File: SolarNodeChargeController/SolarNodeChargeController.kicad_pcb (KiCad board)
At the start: 2 copper layers, 60 x 29 mm, 36 parts, among them J1 Solar_5V, J2 Solar_5V, J3 Solar_5V, J4 Solar_5V, J5 LiPo_1S_4.2V, J6 VOUT, J7 SW_BATT, J8 SW_LOAD, J9 I2C_MCU, Q1 AO3401A, SW3 SOLAR / BATT, U1 CN3791, U2 INA219AID

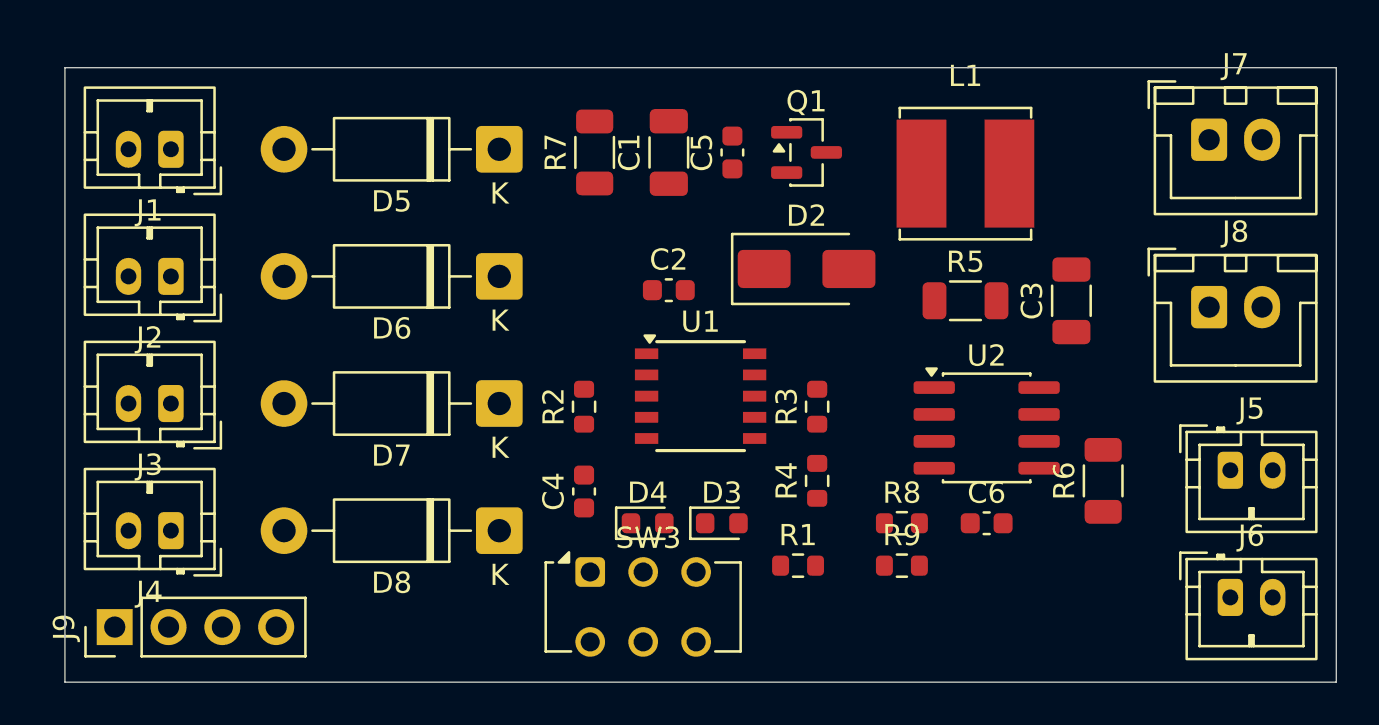
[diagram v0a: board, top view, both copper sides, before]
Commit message: feat: shrink board to 42x26 mm with SMD diodes and 1.25 mm connectors
Input diodes: D5-D8 move from DO-41 1N5819 to SOD-323 1N5819WS (same
40V/1A rating and pinout). The panels peak at ~200-300 mA each, so the
large through-hole part bought nothing and cost ~12 mm of board width.

Connectors: every power connector (solar J1-J4, battery J5, VOUT J6,
switch leads J7/J8) becomes a 2-pin Micro JST 1.25 / Molex PicoBlade
vertical header (53047-0210), and the I2C header J9 a 4-pin one
(53047-0410). The trade-off is that power connectors are no longer
keyed against each other, so the docs call for clear silkscreen labels.

Charge current: R5 0.12R -> 0.15R lowers it from 1.0 A to 0.8 A, leaving
margin on the 1.0 A-rated PicoBlade contacts on the battery path.

The placement draft is rebuilt around the smaller parts: 60x29 -> 42x26
mm, 0 courtyard overlaps, 0 schematic-parity issues, ERC clean.

gen-schematic.js now derives UUIDs from each item's identity (symbol
ref, wire endpoints, label name and position) instead of random ones.
Regenerating an unchanged design is byte-identical, and symbol UUIDs,
which the PCB footprints link to, no longer churn on every run.

README, CLAUDE.md and the README images are updated to match. The
.kicad_pro change is KiCad writing its default settings when the
project was opened.

Co-Authored-By: Claude Opus 5.5 <noreply@anthropic.com>
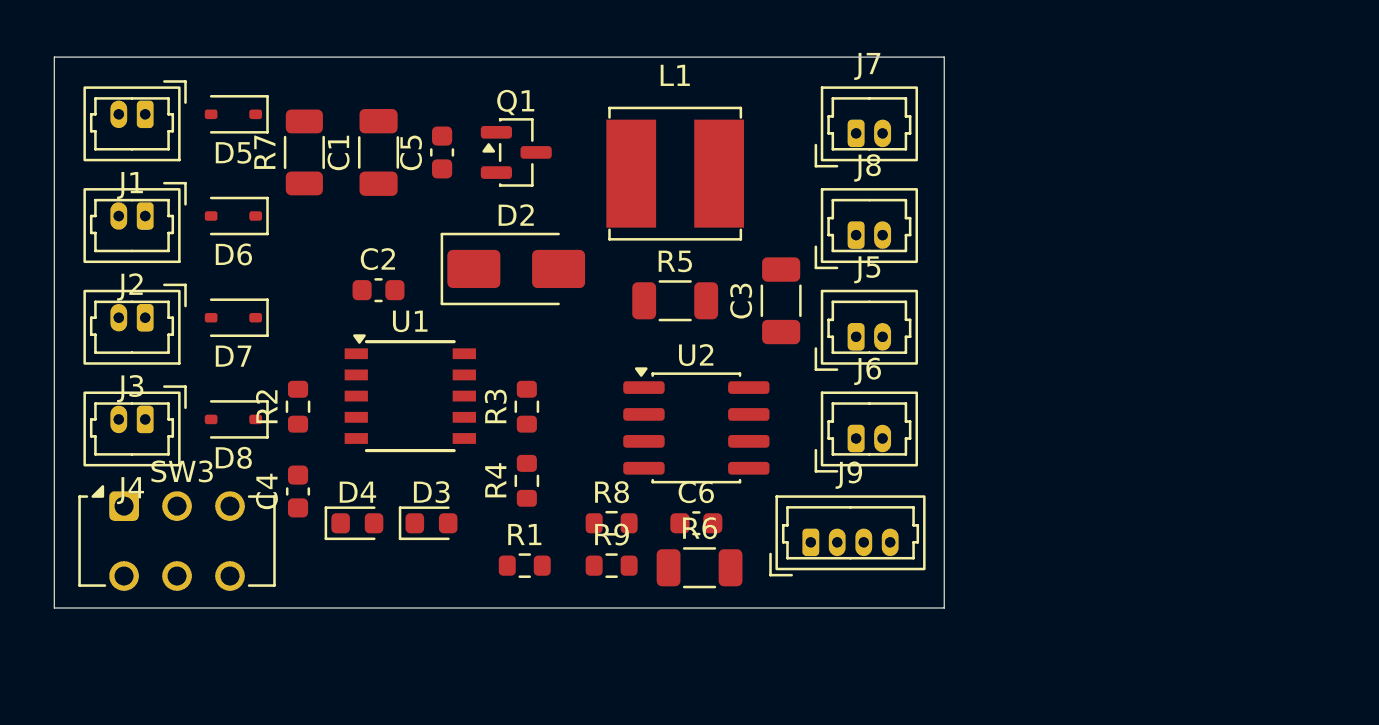
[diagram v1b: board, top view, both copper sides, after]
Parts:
- D5, D6, D7, D8: value 1N5819 -> 1N5819WS; footprint Diode_THT:D_DO-41_SOD81_P10.16mm_Horizontal -> Diode_SMD:D_SOD-323
- J1, J2, J3, J4, J5, J6: footprint Connector_JST:JST_PH_B2B-PH-K_1x02_P2.00mm_Vertical -> Connector_Molex:Molex_PicoBlade_53047-0210_1x02_P1.25mm_Vertical
- J7, J8: footprint Connector_JST:JST_XH_B2B-XH-A_1x02_P2.50mm_Vertical -> Connector_Molex:Molex_PicoBlade_53047-0210_1x02_P1.25mm_Vertical
- J9: footprint Connector_PinHeader_2.54mm:PinHeader_1x04_P2.54mm_Vertical -> Connector_Molex:Molex_PicoBlade_53047-0410_1x04_P1.25mm_Vertical
- R5: value 0.12R 1% -> 0.15R 1%
- moved J9 33.1 mm to (135.2, 122.4), turned to 0 degrees
- moved SW3 22.2 mm to (102.8, 120.7)
- moved R6 19.5 mm to (129.9, 123.6), turned to 0 degrees
- moved J6 19.2 mm to (137.3, 117.5)
- moved J5 18.8 mm to (137.3, 112.7)
- moved J8 17.0 mm to (137.3, 107.9)
- moved J7 16.7 mm to (137.3, 103.1)
- moved C1 13.7 mm to (114.8, 104.0)
- moved C2 13.7 mm to (114.8, 110.5)
- moved C5 13.7 mm to (117.8, 104.0)
- moved D2 13.7 mm to (121.3, 109.5)
- moved D3 13.7 mm to (117.3, 121.5)
- moved D4 13.7 mm to (113.8, 121.5)
- moved Q1 13.7 mm to (121.3, 104.0)
- moved R3 13.7 mm to (121.8, 116.0)
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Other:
- board size 60 x 29 mm -> 42 x 26 mm

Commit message: feat(pcb): route the board, add M3 holes, silkscreen and fab packaging
Board: grows to 56.5 x 29 mm with 2 mm corner chamfers and four
non-plated M3 holes (H1-H4, added to the schematic as MountingHole
symbols, excluded from the BOM). The holes sit in 7.5 mm end bands that
also take SW3 and the I2C connector J9.

Routing: tools/route-pcb.py is a grid A* router written for this board,
since no FreeRouting/Java is available here. It fans GND out first (an
F.Cu stub and via per SMD GND pad; routing signals first left U2 pin 6
boxed in), routes power nets at 0.8 mm (0.4 mm into small pads) and
signals at 0.25 mm, Kelvin-connects the sense pins to R5/R6/R7, and pours
GND on both layers. A turn penalty keeps runs straight/45 degrees, and
B.Cu/via costs keep 80% of copper on F.Cu so the plane stays mostly
whole. Result: 206 segments, 45 vias; DRC 0 violations, 0 unconnected,
schematic parity 0. Power-connector GND pins connect solidly to the
pours, which also fixes starved thermals on the small PicoBlade pads.

Silkscreen: place-pcb.py now places every reference label itself (first
clear side, fine nudges) instead of leaving library positions that
overlapped neighbours. Function labels SW_BATT/SW_LOAD/BATT/VOUT/I2C, one
Solar_5V label with a bracket over J1-J4, I2C pin names and a
"solar/batt / i2c power sensor" label for SW3 on the back (solar at the
PV throws), and the module ID "Solar Charge Module v1.0 / by
JaisorGadgets / Oct. 2026" on the back.

Fabrication: tools/fab-package.js turns the kicad-cli exports into a
JLCPCB-style BOM/CPL, writes fab notes and zips Gerbers + drill files.
The package itself stays in gitignored output/ for a release tag.

gen-schematic.js copies each symbol's in_bom flag from its library, which
keeps parity clean for the mounting holes. README and CLAUDE.md cover the
full regeneration pipeline, routing, labels and fabrication; images are
re-rendered, including a new bottom view. The .kicad_pro change is KiCad
saving its default settings.

C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
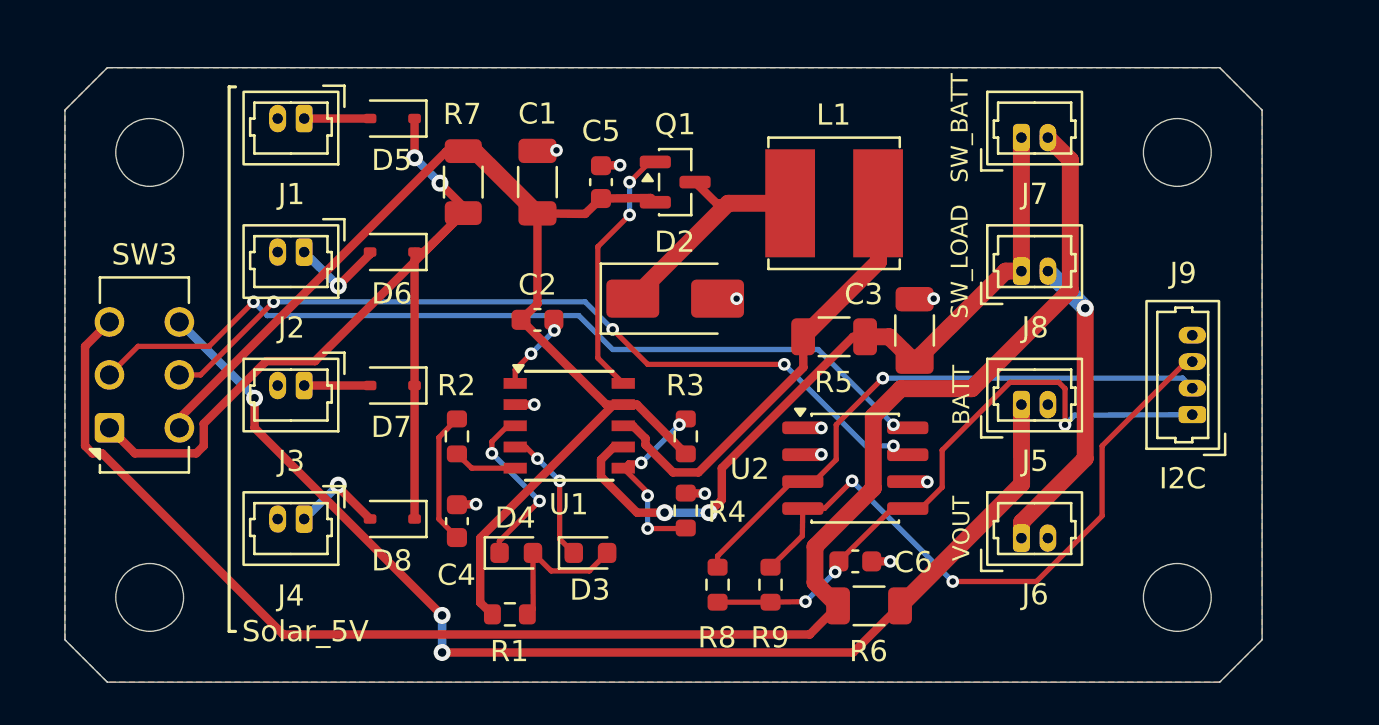
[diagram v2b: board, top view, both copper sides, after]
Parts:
- added H1: M3, MountingHole:MountingHole_3.2mm_M3, F.Cu at (104.0, 104.0)
- added H2: M3, MountingHole:MountingHole_3.2mm_M3, F.Cu at (152.5, 104.0)
- added H3: M3, MountingHole:MountingHole_3.2mm_M3, F.Cu at (104.0, 125.0)
- added H4: M3, MountingHole:MountingHole_3.2mm_M3, F.Cu at (152.5, 125.0)
- moved J9 19.0 mm to (153.2, 116.4), turned to 90 degrees
- moved J6 9.11 mm to (145.1, 122.2)
- moved D8 8.85 mm to (115.5, 121.3)
- moved J4 8.85 mm to (111.3, 121.3)
- moved J5 8.43 mm to (145.1, 115.9)
- moved R6 8.20 mm to (137.9, 125.4)
- moved D7 8.15 mm to (115.5, 115.0)
- moved J3 8.15 mm to (111.3, 115.0)
- moved J8 7.98 mm to (145.1, 109.6)
- moved J7 7.80 mm to (145.1, 103.3)
- moved U2 7.74 mm to (137.3, 118.9)
- moved C6 7.71 mm to (137.3, 123.3)
- moved D6 7.69 mm to (115.5, 108.7)
- moved R5 7.69 mm to (136.3, 112.7)
- moved J2 7.69 mm to (111.3, 108.7)
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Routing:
- net /BATT+: track 0.00 -> 76.1 mm
- net /VIN: track 0.00 -> 58.7 mm
- net /BAT_CELL: track 0.00 -> 55.1 mm, vias 0 -> 3
- net /PV: track 0.00 -> 43.6 mm, vias 0 -> 2
- net /SENSE+: track 0.00 -> 41.6 mm, vias 0 -> 2
- net /SENSE-: track 0.00 -> 38.8 mm, vias 0 -> 4
- net /VBAT: track 0.00 -> 35.5 mm, vias 0 -> 2
- net /SCL: track 0.00 -> 30.5 mm, vias 0 -> 2
- net /VCC_MCU: track 0.00 -> 29.9 mm, vias 0 -> 3
- net /SDA: track 0.00 -> 27.6 mm, vias 0 -> 1
- net /CSP: track 0.00 -> 20.9 mm
- net /VOUT: track 0.00 -> 14.6 mm, vias 0 -> 1
- net Net-(D2-K): track 0.00 -> 14.2 mm
- net /DRV: track 0.00 -> 12.2 mm, vias 0 -> 2
- net GND: track 0.00 -> 9.85 mm, vias 0 -> 11
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- added copper zone on B.Cu, net GND
- added copper zone on F.Cu, net GND
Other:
- board size 42 x 26 mm -> 56.5 x 29 mm
- board text added: "BATT"
- board text added: "GND"
- board text added: "I2C"
- board text added: "Oct. 2026"
- board text added: "SCL"
- board text added: "SDA"
- board text added: "SW_BATT"
- board text added: "SW_LOAD"
- board text added: "Solar Charge Module v1.0"
- board text added: "Solar_5V"
- board text added: "VCC"
- board text added: "VOUT"
- board text added: "by JaisorGadgets"
- board text added: "i2c power sensor"
- board text added: "solar/batt"
